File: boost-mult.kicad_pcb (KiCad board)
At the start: 2 copper layers, 19 x 100 mm, 29 parts, among them J1 IN, J2 OUT1, J3 OUT2, J4 OUT3, J5 OUT4, J6 PWR, SW1 AC_COUPLE, SW2 DRIVE, U1 TL074, U2 TL072

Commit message: wip mounting hole for standoff
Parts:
- added REF**: MountingHole_3.2mm_M3, MountingHole:MountingHole_3.2mm_M3, F.Cu at (124.1, 71.9)
- moved J6 6.89 mm to (127.9, 67.7), turned to 90 degrees
- moved D5 1.14 mm to (133.1, 63.6)
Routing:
- net -12V: track 85.6 -> 78.4 mm
- net /pwr-eurorack-10p/+12V_IN: track 3.72 -> 8.84 mm
- net +12V: track 65.6 -> 63.1 mm
- net GND: track 10.6 -> 11.9 mm

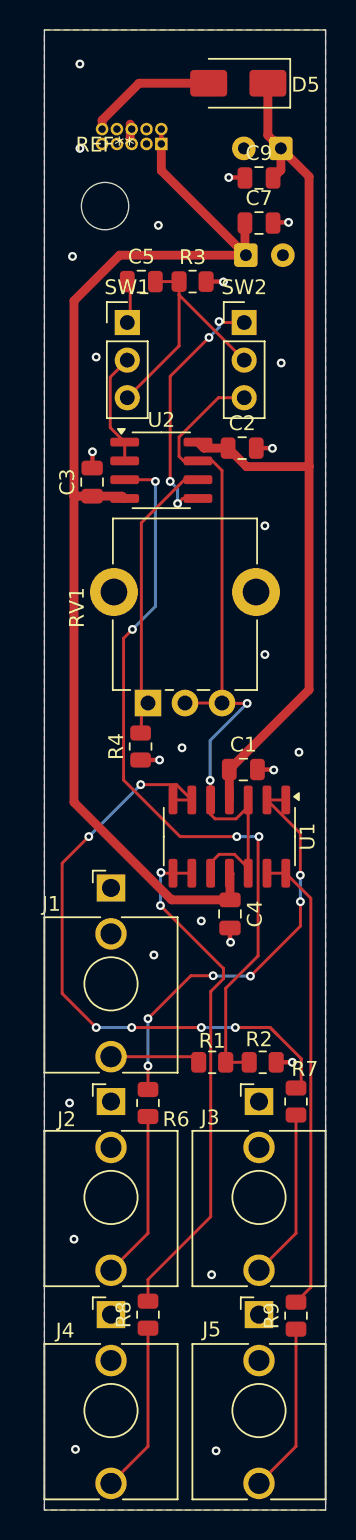
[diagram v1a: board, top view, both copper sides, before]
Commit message: fixing DRC errors
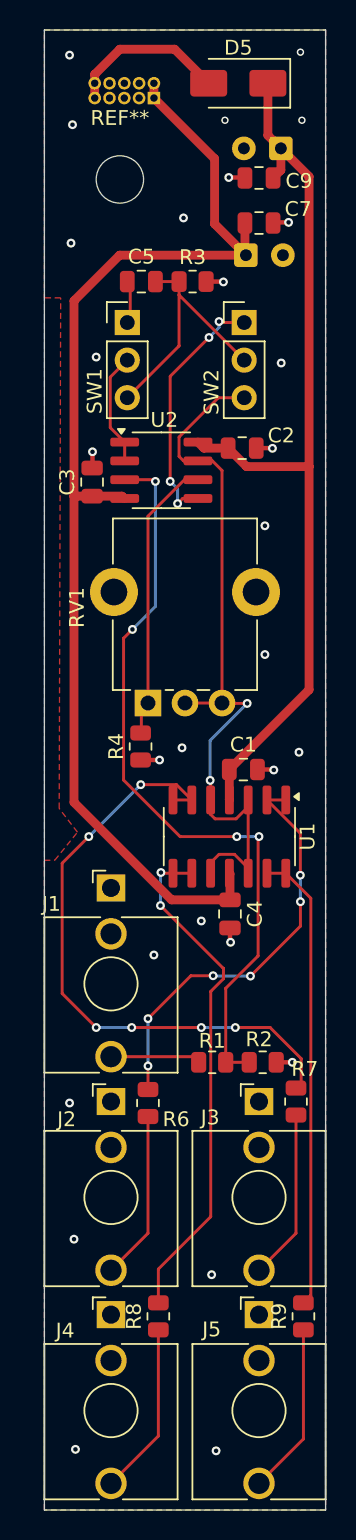
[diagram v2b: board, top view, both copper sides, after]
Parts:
- moved J6 3.14 mm to (127.4, 64.6)
- moved REF** 2.06 mm to (125.1, 70.1)
- moved R8 0.71 mm to (127.7, 146.9)
- moved R9 0.50 mm to (137.5, 146.9)
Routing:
- net -12V: track 78.4 -> 81.7 mm
- net /pwr-eurorack-10p/+12V_IN: track 8.84 -> 12.0 mm
- net GND: track 11.9 -> 10.6 mm, vias 26 -> 29
- net Net-(U1B--): track 45.3 -> 44.6 mm
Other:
- board text added: "STRIPE"

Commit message: holes
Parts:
- added REF**: MountingHole_3mm, MountingHole:MountingHole_3mm, F.Cu at (124.5, 153.3)
- added REF**: MountingHole_3mm, MountingHole:MountingHole_3mm, F.Cu at (124.5, 138.9)
- added REF**: MountingHole_3mm, MountingHole:MountingHole_3mm, F.Cu at (134.5, 153.3)
- added REF**: MountingHole_3mm, MountingHole:MountingHole_3mm, F.Cu at (134.5, 138.9)
- added REF**: MountingHole_3mm, MountingHole:MountingHole_3mm, F.Cu at (124.5, 124.5)

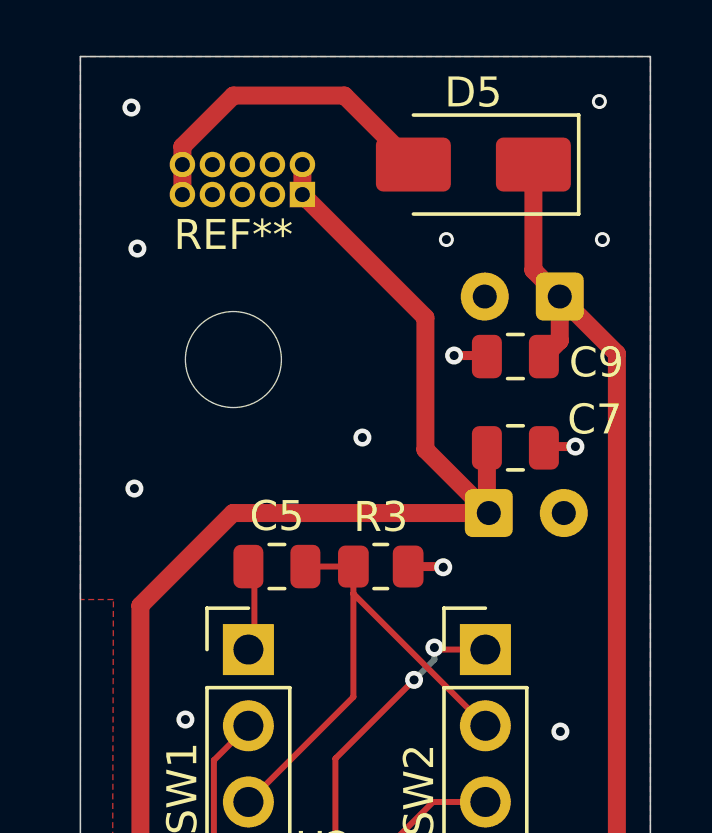
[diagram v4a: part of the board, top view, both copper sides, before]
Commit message: tht film cap, move standoff hole
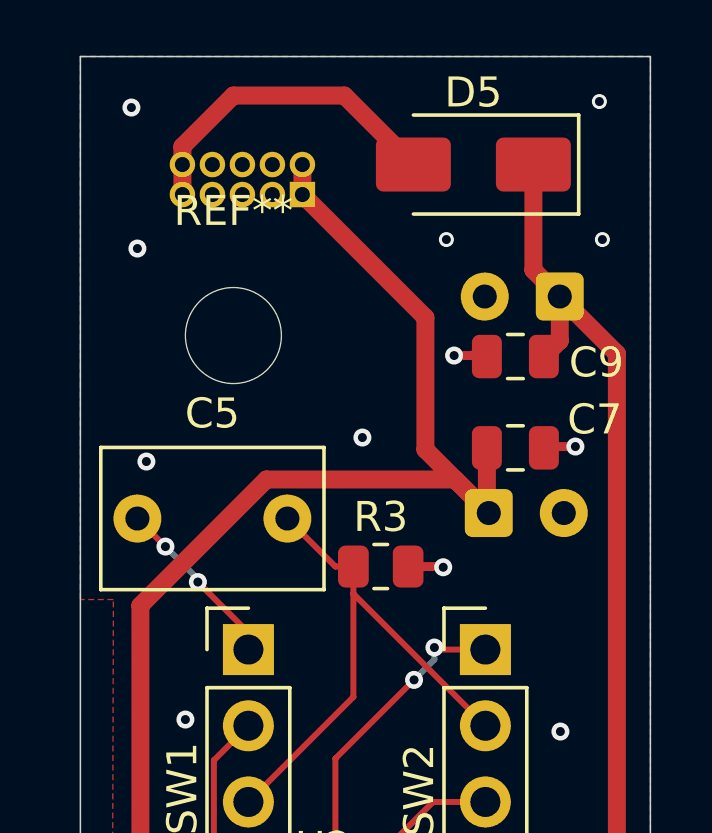
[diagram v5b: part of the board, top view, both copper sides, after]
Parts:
- C5: footprint Capacitor_SMD:C_0805_2012Metric -> Capacitor_THT:C_Rect_L7.2mm_W4.5mm_P5.00mm_FKS2_FKP2_MKS2_MKP2
- moved C5 4.92 mm to (121.9, 75.4)
- moved REF** 0.80 mm to (125.1, 69.3)
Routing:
- net Net-(SW1-A): track 2.83 -> 5.90 mm, vias 0 -> 2
- net Net-(SW1-C): track 17.1 -> 18.4 mm
- net -12V: track 81.7 -> 82.6 mm
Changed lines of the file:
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@@
 		)
 	)
-	(footprint "Capacitor_SMD:C_0805_2012Metric"
+	(footprint "Capacitor_THT:C_Rect_L7.2mm_W4.5mm_P5.00mm_FKS2_FKP2_MKS2_MKP2"
 		(layer "F.Cu")
-		(at 126.55 77)
-		(descr "Capacitor SMD 0805 (2012 Metric), square (rectangular) end terminal, IPC-7351 nominal, (Body size source: IPC-SM-782 page 76, https://www.pcb-3d.com/wordpress/wp-content/uploads/ipc-sm-782a_amendment_1_and_2.pdf, https://docs.google.com/spreadsheets/d/1BsfQQcO9C6DZCsRaXUlFlo91Tg2WpOkGARC1WS5S8t0/edit?usp=sharing), generated with kicad-footprint-generator")
-		(tags "capacitor")
+		(at 121.9 75.4)
+		(descr "C, Rect series, Radial, pin pitch=5.00mm, length*width=7.2*4.5mm^2, Capacitor, http://www.wima.com/EN/WIMA_FKS_2.pdf")
+		(tags "C Rect series Radial pin pitch 5.00mm length 7.2mm width 4.5mm Capacitor")
 		(property "Reference" "C5"
-			(at 0 -1.68 0)
+			(at 2.5 -3.5 0)
 			(layer "F.SilkS")
 			(effects
@@
 		)
 		(property "Value" "1uF"
-			(at 0 1.68 0)
+			(at 2.5 3.5 0)
 			(layer "F.Fab")
 			(effects
@@
 		(sheetname "/")
 		(sheetfile "boost-mult.kicad_sch")
-		(attr smd)
+		(attr through_hole)
 		(fp_line
-			(start -0.261252 -0.735)
-			(end 0.261252 -0.735)
+			(start -1.22 -2.37)
+			(end 6.22 -2.37)
 			(stroke
 				(width 0.12)
@@
 		)
 		(fp_line
-			(start -0.261252 0.735)
-			(end 0.261252 0.735)
+			(start -1.22 2.37)
+			(end -1.22 -2.37)
 			(stroke
 				(width 0.12)
@@
 		)
 		(fp_line
-			(start -1.7 -0.98)
-			(end 1.7 -0.98)
-			(stroke
-				(width 0.05)
-				(type solid)
-			)
-			(layer "F.CrtYd")
-		)
-		(fp_line
-			(start -1.7 0.98)
-			(end -1.7 -0.98)
+			(start 6.22 -2.37)
+			(end 6.22 2.37)
 			(stroke
-				(width 0.05)
+				(width 0.12)
 				(type solid)
 			)
-			(layer "F.CrtYd")
+			(layer "F.SilkS")
 		)
 		(fp_line
-			(start 1.7 -0.98)
-			(end 1.7 0.98)
+			(start 6.22 2.37)
+			(end -1.22 2.37)
 			(stroke
-				(width 0.05)
+				(width 0.12)
 				(type solid)
 			)
-			(layer "F.CrtYd")
+			(layer "F.SilkS")
 		)
-		(fp_line
-			(start 1.7 0.98)
-			(end -1.7 0.98)
+		(fp_rect
+			(start -1.35 -2.5)
+			(end 6.35 2.5)
 			(stroke
 				(width 0.05)
 				(type solid)
 			)
+			(fill no)
 			(layer "F.CrtYd")
 		)
-		(fp_line
-			(start -1 -0.625)
-			(end 1 -0.625)
-			(stroke
-				(width 0.1)
-				(type solid)
-			)
-			(layer "F.Fab")
-		)
-		(fp_line
-			(start -1 0.625)
-			(end -1 -0.625)
-			(stroke
-				(width 0.1)
-				(type solid)
-			)
-			(layer "F.Fab")
-		)
-		(fp_line
-			(start 1 -0.625)
-			(end 1 0.625)
-			(stroke
-				(width 0.1)
-				(type solid)
-			)
-			(layer "F.Fab")
-		)
-		(fp_line
-			(start 1 0.625)
-			(end -1 0.625)
+		(fp_rect
+			(start -1.1 -2.25)
+			(end 6.1 2.25)
 			(stroke
 				(width 0.1)
 				(type solid)
 			)
+			(fill no)
 			(layer "F.Fab")
 		)
 		(fp_text user "${REFERENCE}"
-			(at 0 0 0)
+			(at 2.5 0 0)
 			(layer "F.Fab")
 			(effects
 				(font
-					(size 0.5 0.5)
-					(thickness 0.08)
+					(size 1 1)
+					(thickness 0.15)
 				)
 			)
 		)
-		(pad "1" smd roundrect
-			(at -0.95 0)
-			(size 1 1.45)
-			(layers "F.Cu" "F.Mask" "F.Paste")
-			(roundrect_rratio 0.25)
+		(pad "1" thru_hole circle
+			(at 0 0)
+			(size 1.6 1.6)
+			(drill 0.8)
+			(layers "*.Cu" "*.Mask")
+			(remove_unused_layers no)
 			(net 5 "Net-(SW1-A)")
 			(pintype "passive")
 		)
-		(pad "2" smd roundrect
-			(at 0.95 0)
-			(size 1 1.45)
-			(layers "F.Cu" "F.Mask" "F.Paste")
-			(roundrect_rratio 0.25)
+		(pad "2" thru_hole circle
+			(at 5 0)
+			(size 1.6 1.6)
+			(drill 0.8)
+			(layers "*.Cu" "*.Mask")
+			(remove_unused_layers no)
 			(net 4 "Net-(SW1-C)")
 			(pintype "passive")
 		)
 		(embedded_fonts no)
-		(model "${KICAD9_3DMODEL_DIR}/Capacitor_SMD.3dshapes/C_0805_2012Metric.step"
+		(model "${KICAD9_3DMODEL_DIR}/Capacitor_THT.3dshapes/C_Rect_L7.2mm_W4.5mm_P5.00mm_FKS2_FKP2_MKS2_MKP2.step"
 			(offset
 				(xyz 0 0 0)
@@
 	(footprint "MountingHole:MountingHole_3.2mm_M3"
 		(layer "F.Cu")
-		(at 125.1 70.1)
+		(at 125.1 69.3)
 		(descr "Mounting Hole 3.2mm, M3, no annular, generated by kicad-footprint-generator mountinghole.py")
 		(tags "mountinghole M3")
@@
 	)
 	(via
-		(at 121.8 74.4)
+		(at 122.2 73.5)
 		(size 0.6)
 		(drill 0.3)
@@
 	)
 	(segment
-		(start 125.083787 75.216213)
+		(start 126.201 74.099)
 		(end 122 78.3)
 		(width 0.6)
@@
 	)
 	(segment
-		(start 133.614344 75.216213)
-		(end 125.083787 75.216213)
-		(width 0.6)
-		(layer "F.Cu")
-		(net 3)
-	)
-	(segment
 		(start 128.59019 118.775)
 		(end 132.54 118.775)
@@
 	)
 	(segment
+		(start 133.614344 75.216213)
+		(end 132.497131 74.099)
+		(width 0.6)
+		(layer "F.Cu")
+		(net 3)
+	)
+	(segment
 		(start 132.54 118.775)
 		(end 132.54 117.015)
@@
 	)
 	(segment
+		(start 132.497131 74.099)
+		(end 126.201 74.099)
+		(width 0.6)
+		(layer "F.Cu")
+		(net 3)
+	)
+	(segment
 		(start 122.002723 91.497277)
 		(end 123.223662 91.497277)
@@
 	)
 	(segment
-		(start 127.5 77)
-		(end 129.1 77)
+		(start 126.9 75.4)
+		(end 128.5 77)
 		(width 0.2)
 		(layer "F.Cu")
@@
 	)
 	(segment
+		(start 128.5 77)
+		(end 129.1 77)
+		(width 0.2)
+		(layer "F.Cu")
+		(net 4)
+	)
+	(segment
 		(start 133.4995 82.307375)
 		(end 129.1 77.907875)
@@
 	)
 	(segment
-		(start 125.8 77.2)
-		(end 125.6 77)
+		(start 122.834314 76.334314)
+		(end 121.9 75.4)
 		(width 0.2)
 		(layer "F.Cu")
@@
 	)
 	(segment
-		(start 125.8 79.75)
-		(end 125.8 77.2)
+		(start 125.6 79.2)
+		(end 123.915686 77.515686)
 		(width 0.2)
 		(layer "F.Cu")
 		(net 5)
 	)
+	(segment
+		(start 125.6 79.767375)
+		(end 125.6 79.2)
+		(width 0.2)
+		(layer "F.Cu")
+		(net 5)
+	)
+	(via
+		(at 123.915686 77.515686)
+		(size 0.6)
+		(drill 0.3)
+		(layers "F.Cu" "B.Cu")
+		(net 5)
+	)
+	(via
+		(at 122.834314 76.334314)
+		(size 0.6)
+		(drill 0.3)
+		(layers "F.Cu" "B.Cu")
+		(net 5)
+	)
+	(segment
+		(start 123.915686 77.515686)
+		(end 123.915686 77.415686)
+		(width 0.2)
+		(layer "B.Cu")
+		(net 5)
+	)
+	(segment
+		(start 123.915686 77.415686)
+		(end 122.834314 76.334314)
+		(width 0.2)
+		(layer "B.Cu")
+		(net 5)
+	)

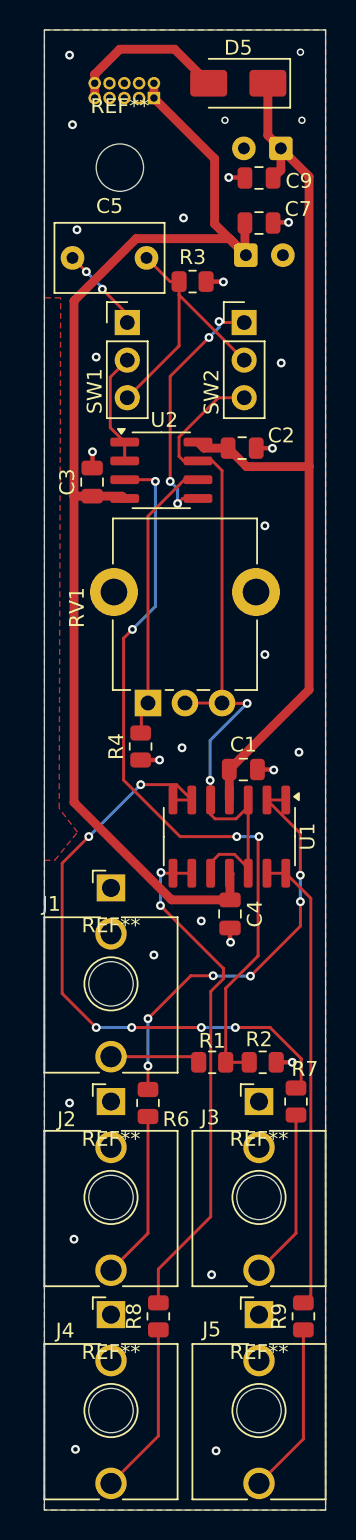
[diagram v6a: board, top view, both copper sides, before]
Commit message: fix incorrect power pin header
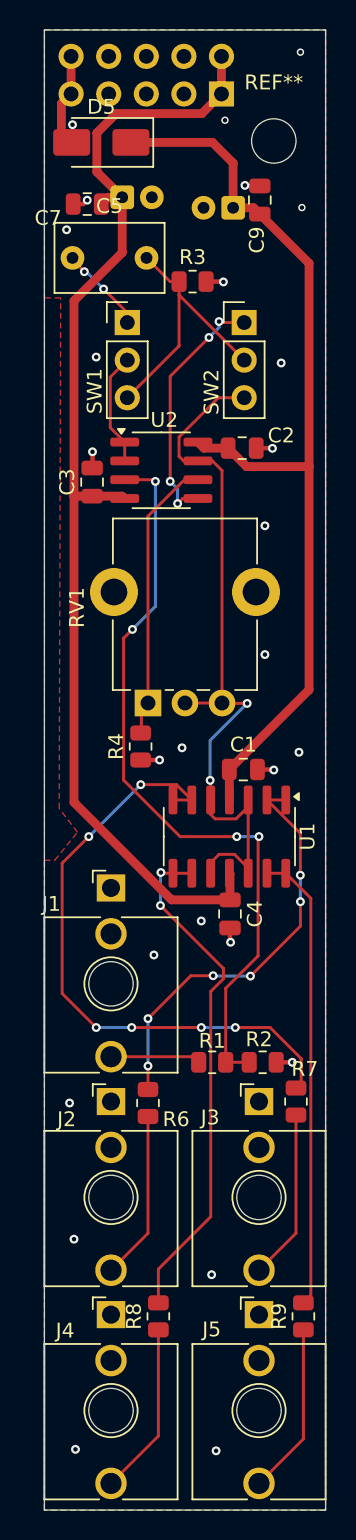
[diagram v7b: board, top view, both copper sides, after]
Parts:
- removed the REF** at (124.5, 153.3)
- removed the REF** at (124.5, 138.9)
- removed the REF** at (125.1, 69.3)
- removed the REF** at (134.5, 153.3)
- removed the REF** at (134.5, 138.9)
- removed the REF** at (124.5, 124.5)
- added REF**: MountingHole_3mm, MountingHole:MountingHole_3mm, F.Cu at (135.5, 67.5)
- C6, C8: footprint Capacitor_THT:CP_Radial_D6.3mm_P2.50mm -> Capacitor_THT:CP_Radial_D5.0mm_P2.00mm
- J6: footprint Connector_PinHeader_1.00mm:PinHeader_2x05_P1.00mm_Vertical -> Connector_PinHeader_2.54mm:PinHeader_2x05_P2.54mm_Vertical
- moved C7 11.7 mm to (122.9, 71.8), turned to 180 degrees
- moved D5 10.1 mm to (123.8, 67.6)
- moved C6 9.23 mm to (125.3, 71.3)
- moved C8 5.15 mm to (132.8, 72.0)
- moved J6 4.57 mm to (132.0, 64.3)
- moved C9 1.49 mm to (134.6, 71.5), turned to -90 degrees
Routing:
- net /pwr-eurorack-10p/+12V_IN: track 12.0 -> 6.37 mm
- net -12V: track 82.6 -> 79.5 mm
- net +12V: track 63.1 -> 63.9 mm
- net GND: track 10.6 -> 9.94 mm, vias 29 -> 27
